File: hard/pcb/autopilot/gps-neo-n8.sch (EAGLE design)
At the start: 18 parts, among them Q1 IRLML5203, T3 BC848

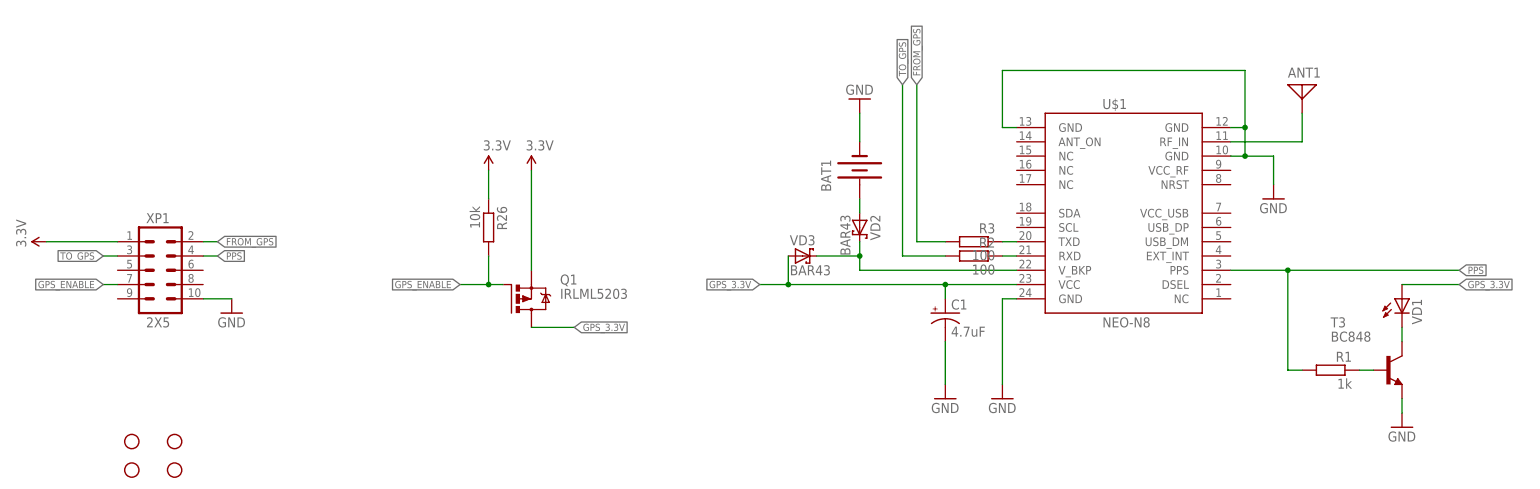
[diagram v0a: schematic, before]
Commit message: update gps NEO board
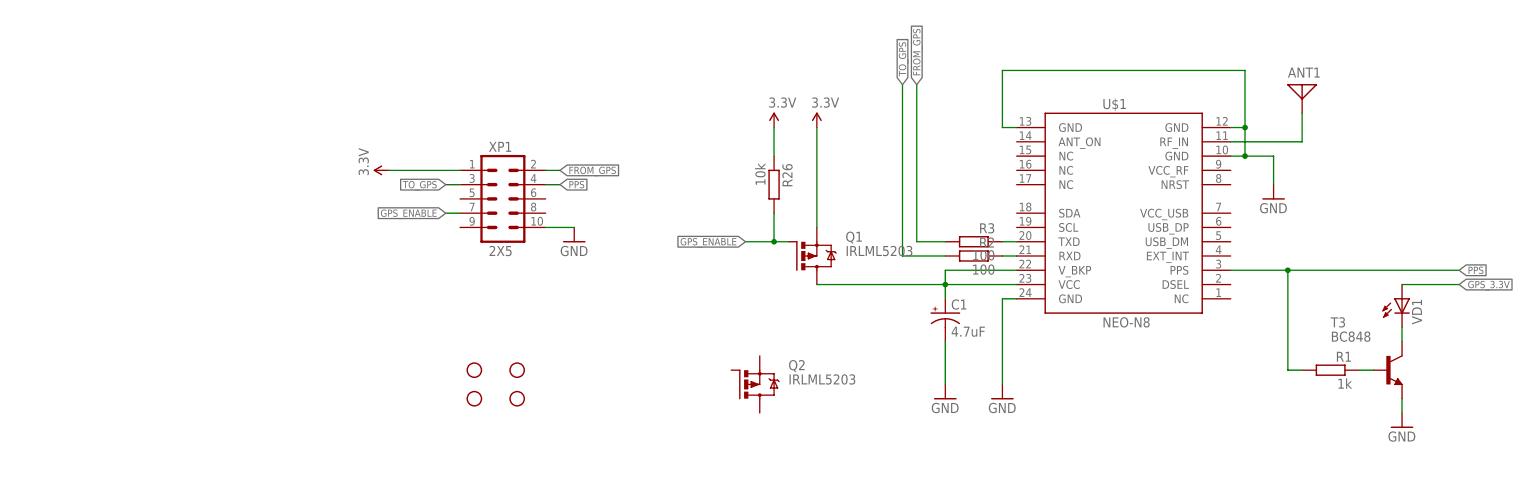
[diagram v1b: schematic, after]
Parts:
- removed BAT1: (no value), SparkFun:BATTERY12MM
- removed VD2, VD3: BAR43, barthess:BAR43
- added Q2: IRLML5203, transistor-power:IRLML5203
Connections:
- removed net N$5: BAT1.+, VD2.A
- removed net N$6: U$1.V_BKP, VD2.C, VD3.C
- net GND: no longer BAT1.-
- net GPS_3.3V: now also U$1.V_BKP; no longer VD3.A
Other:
- moved on the sheet: Q1, R26, XP1
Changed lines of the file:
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@@
 <setting verticaltext="up"/>
 </settings>
-<grid distance="0.1" unitdist="inch" unit="inch" style="lines" multiple="1" display="yes" altdistance="0.01" altunitdist="inch" altunit="inch"/>
+<grid distance="0.1" unitdist="inch" unit="inch" style="lines" multiple="1" display="no" altdistance="0.01" altunitdist="inch" altunit="inch"/>
 <layers>
 <layer number="1" name="Top" color="4" fill="1" visible="no" active="no"/>
@@
 <part name="P+16" library="SparkFun" deviceset="3.3V" device=""/>
 <part name="P+17" library="SparkFun" deviceset="3.3V" device=""/>
-<part name="BAT1" library="SparkFun" deviceset="BATTERY" device="12MM"/>
 <part name="XP1" library="barthess" deviceset="2X5" device=""/>
 <part name="C1" library="SparkFun" deviceset="CAP_POL" device="1206-KIT" value="4.7uF"/>
@@
 <part name="VD1" library="barthess" deviceset="LED" device="0805"/>
 <part name="R1" library="rcl" deviceset="R-EU_" device="R0805" value="1k"/>
-<part name="GND3" library="SparkFun" deviceset="GND" device=""/>
-<part name="VD2" library="barthess" deviceset="BAR43" device=""/>
-<part name="VD3" library="barthess" deviceset="BAR43" device=""/>
 <part name="U$1" library="barthess" deviceset="NEO-N8" device=""/>
 <part name="ANT1" library="barthess" deviceset="GPS_ANTENNA" device="'35X35'"/>
@@
 <part name="R2" library="rcl" deviceset="R-EU_" device="R0805" value="100"/>
 <part name="R3" library="rcl" deviceset="R-EU_" device="R0805" value="100"/>
+<part name="Q2" library="transistor-power" deviceset="IRLML5203" device=""/>
 </parts>
 <sheets>
@@
 <instances>
 <instance part="GND25" gate="1" x="114.3" y="17.78"/>
-<instance part="GND26" gate="1" x="-93.98" y="38.1"/>
-<instance part="P+14" gate="G$1" x="-127" y="50.8" rot="R90"/>
-<instance part="Q1" gate="G$1" x="-43.18" y="40.64"/>
-<instance part="R26" gate="G$1" x="-48.26" y="53.34" rot="R270"/>
-<instance part="P+16" gate="G$1" x="-40.64" y="63.5"/>
-<instance part="P+17" gate="G$1" x="-48.26" y="63.5"/>
-<instance part="BAT1" gate="G$1" x="17.78" y="63.5" rot="R90"/>
-<instance part="XP1" gate="G$1" x="-106.68" y="45.72"/>
+<instance part="GND26" gate="1" x="-33.02" y="50.8"/>
+<instance part="P+14" gate="G$1" x="-66.04" y="63.5" rot="R90"/>
+<instance part="Q1" gate="G$1" x="7.62" y="48.26"/>
+<instance part="R26" gate="G$1" x="2.54" y="60.96" rot="R270"/>
+<instance part="P+16" gate="G$1" x="10.16" y="71.12"/>
+<instance part="P+17" gate="G$1" x="2.54" y="71.12"/>
+<instance part="XP1" gate="G$1" x="-45.72" y="58.42"/>
 <instance part="C1" gate="G$1" x="33.02" y="38.1"/>
 <instance part="GND1" gate="1" x="33.02" y="22.86"/>
 <instance part="VD1" gate="G$1" x="114.3" y="40.64"/>
 <instance part="R1" gate="G$1" x="101.6" y="27.94" rot="MR0"/>
-<instance part="GND3" gate="1" x="17.78" y="76.2" rot="MR180"/>
-<instance part="VD2" gate="1" x="17.78" y="53.34" rot="R270"/>
-<instance part="VD3" gate="1" x="7.62" y="48.26"/>
 <instance part="U$1" gate="G$1" x="45.72" y="71.12"/>
 <instance part="ANT1" gate="A" x="96.52" y="78.74"/>
 <instance part="GND4" gate="1" x="43.18" y="22.86"/>
 <instance part="GND5" gate="1" x="91.44" y="58.42"/>
-<instance part="JP1" gate="G$1" x="-111.76" y="10.16" rot="R90"/>
-<instance part="JP2" gate="G$1" x="-111.76" y="15.24" rot="R90"/>
-<instance part="JP4" gate="G$1" x="-104.14" y="10.16" rot="R90"/>
-<instance part="JP5" gate="G$1" x="-104.14" y="15.24" rot="R90"/>
+<instance part="JP1" gate="G$1" x="-50.8" y="22.86" rot="R90"/>
+<instance part="JP2" gate="G$1" x="-50.8" y="27.94" rot="R90"/>
+<instance part="JP4" gate="G$1" x="-43.18" y="22.86" rot="R90"/>
+<instance part="JP5" gate="G$1" x="-43.18" y="27.94" rot="R90"/>
 <instance part="T3" gate="G$1" x="111.76" y="27.94"/>
 <instance part="R2" gate="G$1" x="38.1" y="48.26" rot="MR0"/>
 <instance part="R3" gate="G$1" x="38.1" y="50.8" rot="MR0"/>
+<instance part="Q2" gate="G$1" x="-2.54" y="25.4"/>
 </instances>
 <busses>
@@
 <net name="3.3V" class="0">
 <segment>
-<wire x1="-114.3" y1="50.8" x2="-127" y2="50.8" width="0.1524" layer="91"/>
+<wire x1="-53.34" y1="63.5" x2="-66.04" y2="63.5" width="0.1524" layer="91"/>
 <pinref part="P+14" gate="G$1" pin="3.3V"/>
 <pinref part="XP1" gate="G$1" pin="1"/>
 </segment>
 <segment>
-<wire x1="-40.64" y1="45.72" x2="-40.64" y2="63.5" width="0.1524" layer="91"/>
+<wire x1="10.16" y1="53.34" x2="10.16" y2="71.12" width="0.1524" layer="91"/>
 <pinref part="Q1" gate="G$1" pin="S"/>
 <pinref part="P+16" gate="G$1" pin="3.3V"/>
@@
 <pinref part="R26" gate="G$1" pin="1"/>
 <pinref part="P+17" gate="G$1" pin="3.3V"/>
-<wire x1="-48.26" y1="58.42" x2="-48.26" y2="63.5" width="0.1524" layer="91"/>
+<wire x1="2.54" y1="66.04" x2="2.54" y2="71.12" width="0.1524" layer="91"/>
 </segment>
 </net>
 <net name="GND" class="0">
 <segment>
-<wire x1="-99.06" y1="40.64" x2="-93.98" y2="40.64" width="0.1524" layer="91"/>
+<wire x1="-38.1" y1="53.34" x2="-33.02" y2="53.34" width="0.1524" layer="91"/>
 <pinref part="GND26" gate="1" pin="GND"/>
 <pinref part="XP1" gate="G$1" pin="10"/>
@@
 <pinref part="C1" gate="G$1" pin="-"/>
 <pinref part="GND1" gate="1" pin="GND"/>
-</segment>
-<segment>
-<wire x1="17.78" y1="73.66" x2="17.78" y2="68.58" width="0.1524" layer="91"/>
-<pinref part="BAT1" gate="G$1" pin="-"/>
-<pinref part="GND3" gate="1" pin="GND"/>
 </segment>
 <segment>
@@
 <net name="TO_GPS" class="0">
 <segment>
-<wire x1="-114.3" y1="48.26" x2="-116.84" y2="48.26" width="0.1524" layer="91"/>
-<label x="-116.84" y="48.26" size="1.27" layer="95" rot="R180" xref="yes"/>
+<wire x1="-53.34" y1="60.96" x2="-55.88" y2="60.96" width="0.1524" layer="91"/>
+<label x="-55.88" y="60.96" size="1.27" layer="95" rot="R180" xref="yes"/>
 <pinref part="XP1" gate="G$1" pin="3"/>
 </segment>
@@
 <net name="FROM_GPS" class="0">
 <segment>
-<wire x1="-99.06" y1="50.8" x2="-96.52" y2="50.8" width="0.1524" layer="91"/>
-<label x="-96.52" y="50.8" size="1.27" layer="95" xref="yes"/>
+<wire x1="-38.1" y1="63.5" x2="-35.56" y2="63.5" width="0.1524" layer="91"/>
+<label x="-35.56" y="63.5" size="1.27" layer="95" xref="yes"/>
 <pinref part="XP1" gate="G$1" pin="2"/>
 </segment>
@@
 <net name="PPS" class="0">
 <segment>
-<wire x1="-99.06" y1="48.26" x2="-96.52" y2="48.26" width="0.1524" layer="91"/>
-<label x="-96.52" y="48.26" size="1.27" layer="95" xref="yes"/>
+<wire x1="-38.1" y1="60.96" x2="-35.56" y2="60.96" width="0.1524" layer="91"/>
+<label x="-35.56" y="60.96" size="1.27" layer="95" xref="yes"/>
 <pinref part="XP1" gate="G$1" pin="4"/>
 </segment>
@@
 <net name="GPS_ENABLE" class="0">
 <segment>
-<label x="-53.34" y="43.18" size="1.27" layer="95" rot="R180" xref="yes"/>
+<label x="-2.54" y="50.8" size="1.27" layer="95" rot="R180" xref="yes"/>
 <pinref part="R26" gate="G$1" pin="2"/>
 <pinref part="Q1" gate="G$1" pin="G"/>
-<wire x1="-48.26" y1="43.18" x2="-45.72" y2="43.18" width="0.1524" layer="91"/>
-<wire x1="-48.26" y1="43.18" x2="-48.26" y2="48.26" width="0.1524" layer="91"/>
-<wire x1="-48.26" y1="43.18" x2="-53.34" y2="43.18" width="0.1524" layer="91"/>
-<junction x="-48.26" y="43.18"/>
-</segment>
-<segment>
-<wire x1="-114.3" y1="43.18" x2="-116.84" y2="43.18" width="0.1524" layer="91"/>
-<label x="-116.84" y="43.18" size="1.27" layer="95" rot="R180" xref="yes"/>
+<wire x1="2.54" y1="50.8" x2="5.08" y2="50.8" width="0.1524" layer="91"/>
+<wire x1="2.54" y1="50.8" x2="2.54" y2="55.88" width="0.1524" layer="91"/>
+<wire x1="2.54" y1="50.8" x2="-2.54" y2="50.8" width="0.1524" layer="91"/>
+<junction x="2.54" y="50.8"/>
+</segment>
+<segment>
+<wire x1="-53.34" y1="55.88" x2="-55.88" y2="55.88" width="0.1524" layer="91"/>
+<label x="-55.88" y="55.88" size="1.27" layer="95" rot="R180" xref="yes"/>
 <pinref part="XP1" gate="G$1" pin="7"/>
 </segment>
 </net>
 <net name="GPS_3.3V" class="0">
-<segment>
-<pinref part="Q1" gate="G$1" pin="D"/>
-<wire x1="-40.64" y1="35.56" x2="-33.02" y2="35.56" width="0.1524" layer="91"/>
-<label x="-33.02" y="35.56" size="1.27" layer="95" xref="yes"/>
-</segment>
 <segment>
 <pinref part="C1" gate="G$1" pin="+"/>
@@
 <wire x1="33.02" y1="43.18" x2="33.02" y2="40.64" width="0.1524" layer="91"/>
 <junction x="33.02" y="43.18"/>
-<wire x1="33.02" y1="43.18" x2="5.08" y2="43.18" width="0.1524" layer="91"/>
-<pinref part="VD3" gate="1" pin="A"/>
-<wire x1="5.08" y1="48.26" x2="5.08" y2="43.18" width="0.1524" layer="91"/>
-<junction x="5.08" y="43.18"/>
-<wire x1="5.08" y1="43.18" x2="0" y2="43.18" width="0.1524" layer="91"/>
-<label x="0" y="43.18" size="1.27" layer="95" rot="R180" xref="yes"/>
+<wire x1="33.02" y1="43.18" x2="10.16" y2="43.18" width="0.1524" layer="91"/>
+<pinref part="U$1" gate="G$1" pin="V_BKP"/>
+<wire x1="45.72" y1="45.72" x2="33.02" y2="45.72" width="0.1524" layer="91"/>
+<wire x1="33.02" y1="45.72" x2="33.02" y2="43.18" width="0.1524" layer="91"/>
+<pinref part="Q1" gate="G$1" pin="D"/>
 </segment>
 <segment>
@@
 </segment>
 </net>
-<net name="N$5" class="0">
-<segment>
-<wire x1="17.78" y1="58.42" x2="17.78" y2="55.88" width="0.1524" layer="91"/>
-<pinref part="BAT1" gate="G$1" pin="+"/>
-<pinref part="VD2" gate="1" pin="A"/>
-</segment>
-</net>
-<net name="N$6" class="0">
-<segment>
-<wire x1="17.78" y1="50.8" x2="17.78" y2="48.26" width="0.1524" layer="91"/>
-<wire x1="17.78" y1="48.26" x2="17.78" y2="45.72" width="0.1524" layer="91"/>
-<wire x1="10.16" y1="48.26" x2="17.78" y2="48.26" width="0.1524" layer="91"/>
-<junction x="17.78" y="48.26"/>
-<pinref part="VD2" gate="1" pin="C"/>
-<pinref part="VD3" gate="1" pin="C"/>
-<pinref part="U$1" gate="G$1" pin="V_BKP"/>
-<wire x1="17.78" y1="45.72" x2="45.72" y2="45.72" width="0.1524" layer="91"/>
-</segment>
-</net>
